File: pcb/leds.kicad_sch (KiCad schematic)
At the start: 53 parts, among them J5 Conn_01x03_Pin, J6 Conn_01x03_Socket, U2 SN74LVC1T45DBV

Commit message: routing
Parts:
- removed C43, C44, C45, C46, C47, C49, C50: 100n, Capacitor_SMD:C_0603_1608Metric, symbol Device:C_Small
- removed D32, D33, D34, D35, D36: WS2812B, Equilibot:XL_WS2812B_1615, symbol XL_WS2812B_1615:WS2812B
- removed J6: Conn_01x03_Socket, Connector_PinSocket_2.54mm:PinSocket_1x03_P2.54mm_Vertical, symbol Connector:Conn_01x03_Socket
- added TP11: TestPoint, Equilibot:TestPoint_Pad_1.0x1.0mm, symbol Connector:TestPoint
- TP16, TP8: footprint TestPoint:TestPoint_Pad_D1.0mm -> Equilibot:TestPoint_Pad_1.0x1.0mm
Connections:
- net 5V: now also TP11.1
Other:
- moved on the sheet: TP16

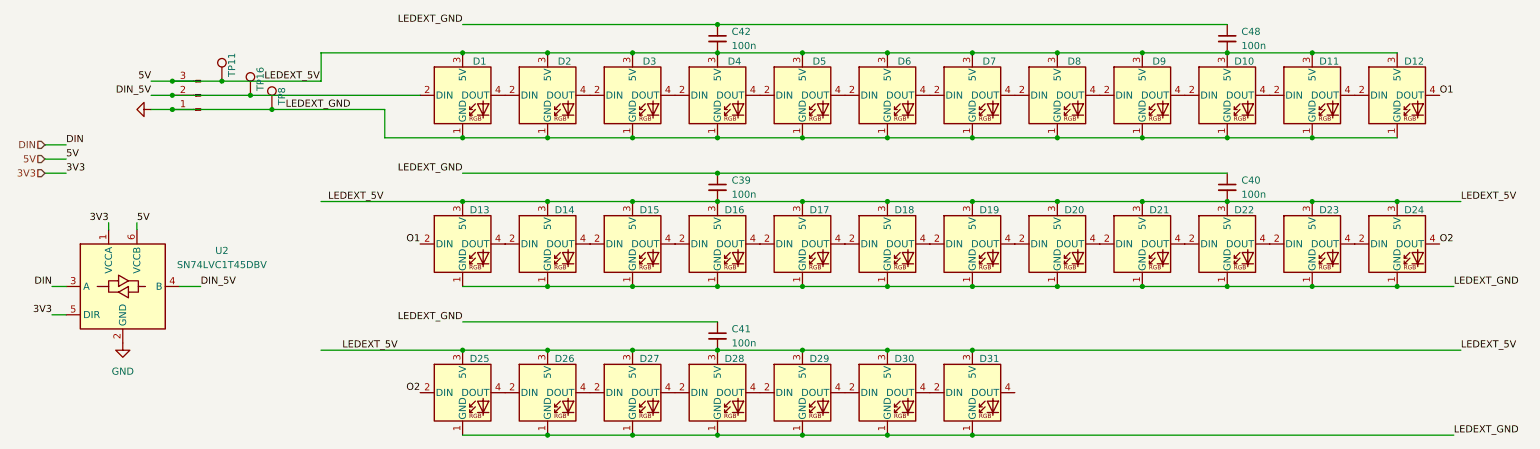
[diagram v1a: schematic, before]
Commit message: add jlcpcb part numbers
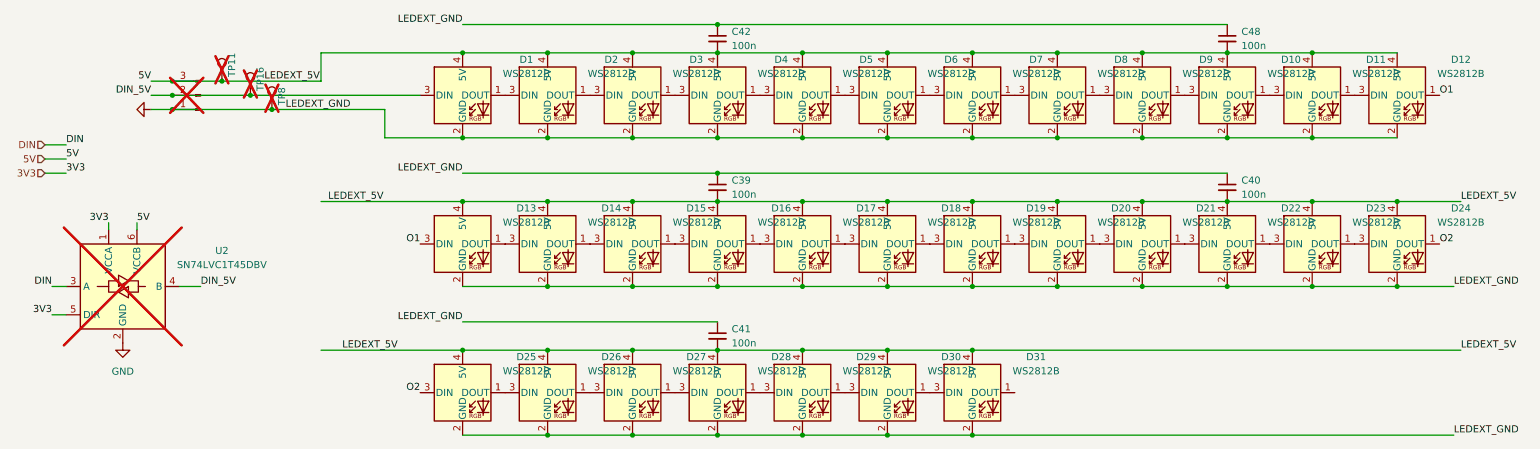
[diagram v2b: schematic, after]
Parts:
- C39, C40, C41, C42, C48: JLCPCB Part (none) -> C14663
- D1, D10, D11, D12, D13, D14, D15, D16, D17, D18, D19, D2, D20, D21, D22, D23, D24, D25, D26, D27, D28, D29, D3, D30, D31, D4, D5, D6, D7, D8, D9: footprint Equilibot:XL_WS2812B_1615 -> Equilibot:XL_WS2812B_0807; JLCPCB Part (none) -> C3646929
- J5, TP11, TP16, TP8: now not fitted
- U2: JLCPCB Part (none) -> C7843; now not fitted
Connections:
- net 5V: now also D1.4 (5V), D10.4 (5V), D11.4 (5V), D12.4 (5V), D13.4 (5V), D14.4 (5V), D15.4 (5V), D16.4 (5V), D17.4 (5V), D18.4 (5V), D19.4 (5V), D2.4 (5V), D20.4 (5V), D21.4 (5V), D22.4 (5V), D23.4 (5V), D24.4 (5V), D25.4 (5V), D26.4 (5V), D27.4 (5V), D28.4 (5V), D29.4 (5V), D3.4 (5V), D30.4 (5V), D31.4 (5V), D4.4 (5V), D5.4 (5V), D6.4 (5V), D7.4 (5V), D8.4 (5V), D9.4 (5V); no longer D1.3 (5V), D10.3 (5V), D11.3 (5V), D12.3 (5V), D13.3 (5V), D14.3 (5V), D15.3 (5V), D16.3 (5V), D17.3 (5V), D18.3 (5V), D19.3 (5V), D2.3 (5V), D20.3 (5V), D21.3 (5V), D22.3 (5V), D23.3 (5V), D24.3 (5V), D25.3 (5V), D26.3 (5V), D27.3 (5V), D28.3 (5V), D29.3 (5V), D3.3 (5V), D30.3 (5V), D31.3 (5V), D4.3 (5V), D5.3 (5V), D6.3 (5V), D7.3 (5V), D8.3 (5V), D9.3 (5V)
- net DIN_5V: now also D1.3 (DIN); no longer D1.2 (DIN)
- net GND: now also D1.2 (GND), D10.2 (GND), D11.2 (GND), D12.2 (GND), D13.2 (GND), D14.2 (GND), D15.2 (GND), D16.2 (GND), D17.2 (GND), D18.2 (GND), D19.2 (GND), D2.2 (GND), D20.2 (GND), D21.2 (GND), D22.2 (GND), D23.2 (GND), D24.2 (GND), D25.2 (GND), D26.2 (GND), D27.2 (GND), D28.2 (GND), D29.2 (GND), D3.2 (GND), D30.2 (GND), D31.2 (GND), D4.2 (GND), D5.2 (GND), D6.2 (GND), D7.2 (GND), D8.2 (GND), D9.2 (GND); no longer D1.1 (GND), D10.1 (GND), D11.1 (GND), D12.1 (GND), D13.1 (GND), D14.1 (GND), D15.1 (GND), D16.1 (GND), D17.1 (GND), D18.1 (GND), D19.1 (GND), D2.1 (GND), D20.1 (GND), D21.1 (GND), D22.1 (GND), D23.1 (GND), D24.1 (GND), D25.1 (GND), D26.1 (GND), D27.1 (GND), D28.1 (GND), D29.1 (GND), D3.1 (GND), D30.1 (GND), D31.1 (GND), D4.1 (GND), D5.1 (GND), D6.1 (GND), D7.1 (GND), D8.1 (GND), D9.1 (GND)
- net O1: now also D12.1 (DOUT), D13.3 (DIN); no longer D12.4 (DOUT), D13.2 (DIN)
- net O2: now also D24.1 (DOUT), D25.3 (DIN); no longer D24.4 (DOUT), D25.2 (DIN)
- new net: D10.3 (DIN), D9.1 (DOUT)
- new net: D8.1 (DOUT), D9.3 (DIN)
- new net: D15.1 (DOUT), D16.3 (DIN)
- new net: D14.1 (DOUT), D15.3 (DIN)
- new net: D7.1 (DOUT), D8.3 (DIN)
- new net: D6.1 (DOUT), D7.3 (DIN)
- new net: D23.1 (DOUT), D24.3 (DIN)
- new net: D25.1 (DOUT), D26.3 (DIN)
- new net: D22.1 (DOUT), D23.3 (DIN)
- new net: D21.1 (DOUT), D22.3 (DIN)
- new net: D11.1 (DOUT), D12.3 (DIN)
- new net: D10.1 (DOUT), D11.3 (DIN)
- new net: D27.1 (DOUT), D28.3 (DIN)
- new net: D26.1 (DOUT), D27.3 (DIN)
- new net: D13.1 (DOUT), D14.3 (DIN)
- new net: D5.1 (DOUT), D6.3 (DIN)
- new net: D1.1 (DOUT), D2.3 (DIN)
- new net: D18.1 (DOUT), D19.3 (DIN)
- new net: D17.1 (DOUT), D18.3 (DIN)
- new net: D30.1 (DOUT), D31.3 (DIN)
- new net: D4.1 (DOUT), D5.3 (DIN)
- new net: D3.1 (DOUT), D4.3 (DIN)
- new net: D28.1 (DOUT), D29.3 (DIN)
- new net: D20.1 (DOUT), D21.3 (DIN)
- new net: D19.1 (DOUT), D20.3 (DIN)
- new net: D16.1 (DOUT), D17.3 (DIN)
- new net: D2.1 (DOUT), D3.3 (DIN)
- new net: D29.1 (DOUT), D30.3 (DIN)

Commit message: PRODUCTION
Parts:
- C39, C40, C41, C42, C48: now not fitted
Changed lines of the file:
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@@
 		(in_bom yes)
 		(on_board yes)
-		(dnp no)
+		(dnp yes)
 		(fields_autoplaced yes)
 		(property "Reference" "C39"
@@
 		(in_bom yes)
 		(on_board yes)
-		(dnp no)
+		(dnp yes)
 		(fields_autoplaced yes)
 		(property "Reference" "C48"
@@
 		(in_bom yes)
 		(on_board yes)
-		(dnp no)
+		(dnp yes)
 		(fields_autoplaced yes)
 		(property "Reference" "C42"
@@
 		(in_bom yes)
 		(on_board yes)
-		(dnp no)
+		(dnp yes)
 		(fields_autoplaced yes)
 		(property "Reference" "C41"
@@
 		(in_bom yes)
 		(on_board yes)
-		(dnp no)
+		(dnp yes)
 		(fields_autoplaced yes)
 		(property "Reference" "C40"
